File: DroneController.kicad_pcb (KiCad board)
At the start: 4 copper layers, 50.7 x 56.1 mm, 45 parts, among them J1 Connector, J2 Connector, J3 Connector, P1 USB_C_Plug, SW1 SW_SPDT, U2 W25Q16JVSS, U3 BMP280, U4 MPU-6500, U6 L86-M33, U7 915MHz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

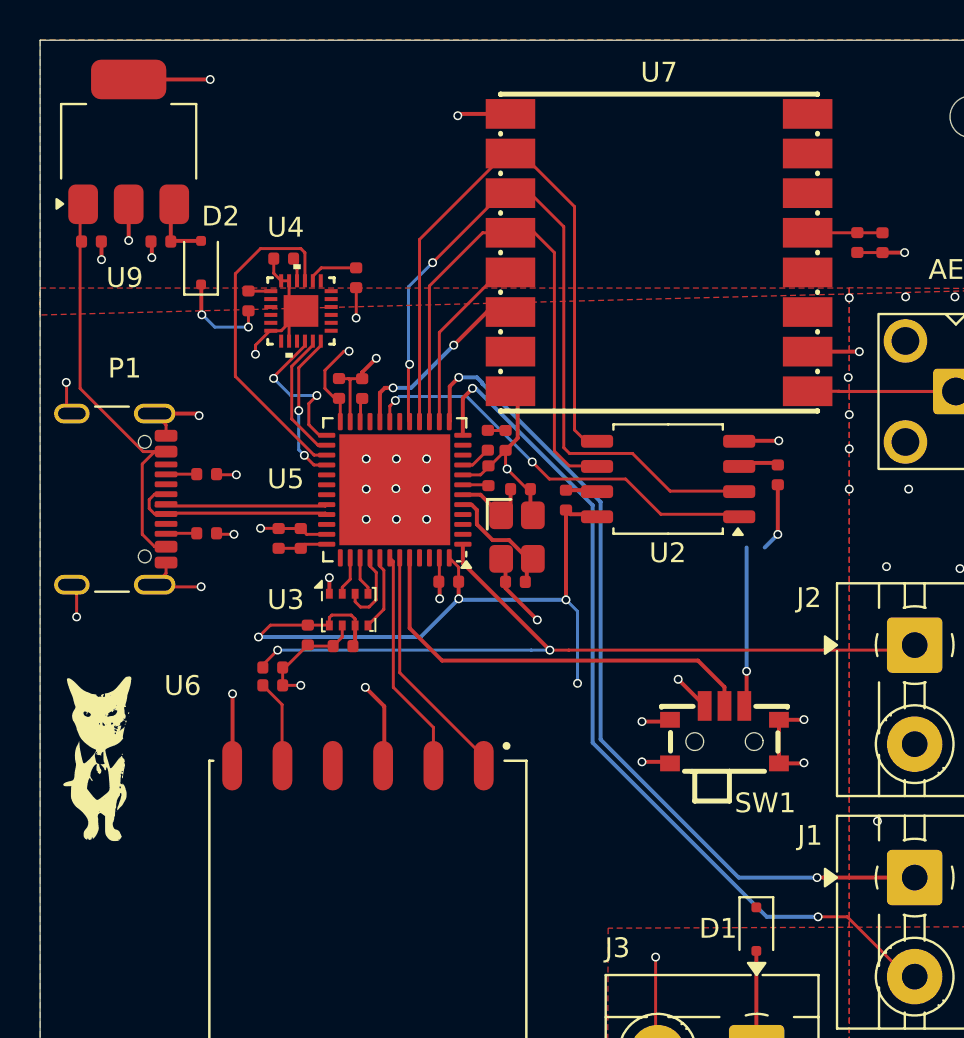
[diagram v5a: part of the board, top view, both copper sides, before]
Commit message: Updated DRC requirements, footprints, and board stackup for impedance management
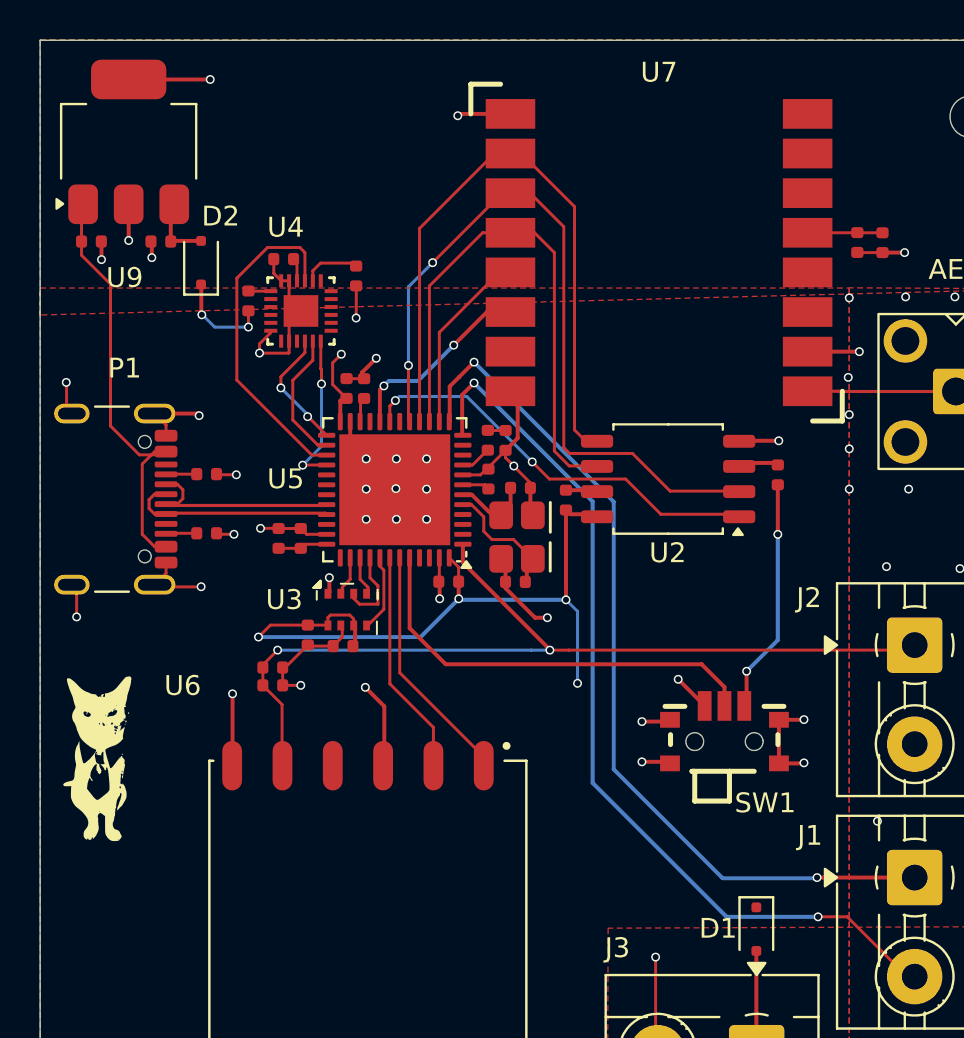
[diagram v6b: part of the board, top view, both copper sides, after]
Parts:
- moved C9 0.38 mm to (116.9, 122.4)
- moved C27 0.17 mm to (124.0, 127.0)
- moved C26 0.10 mm to (117.8, 122.4)
- moved C1 0.09 mm to (117.3, 116.8)
- moved U3 0.07 mm to (116.9, 133.6)
- moved C7 0.06 mm to (125.6, 127.5)
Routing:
- net GND: track 100.7 -> 103.3 mm
- net /USB_FS_DN: track 8.75 -> 10.6 mm
- net /USART2_TX: track 44.2 -> 45.9 mm
- net /SPI2_NSS: track 7.84 -> 6.22 mm
- net /USART2_RX: track 43.0 -> 44.5 mm
- net +BATT: track 45.2 -> 46.1 mm
- net /USB_FS_DP: track 11.2 -> 10.5 mm

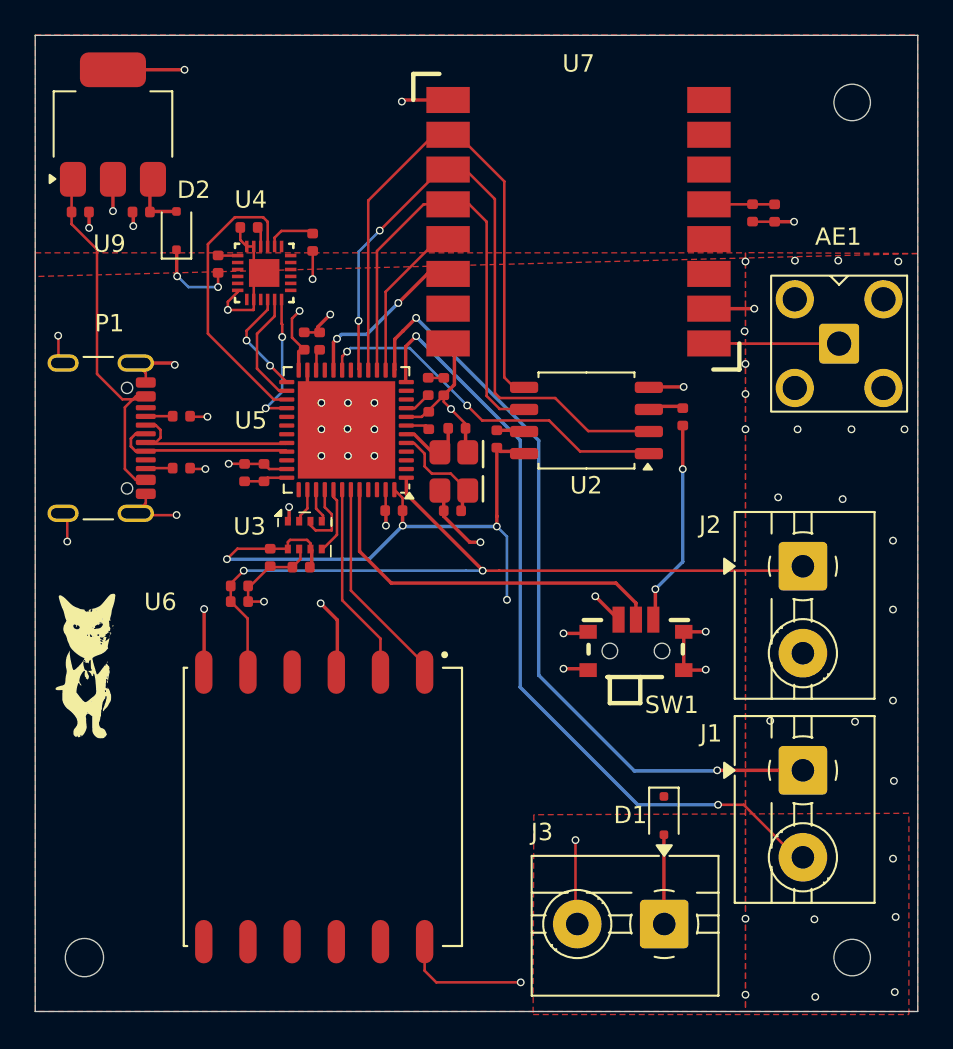
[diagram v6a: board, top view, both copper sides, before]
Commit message: added pull-up resistors, added keepout zones.
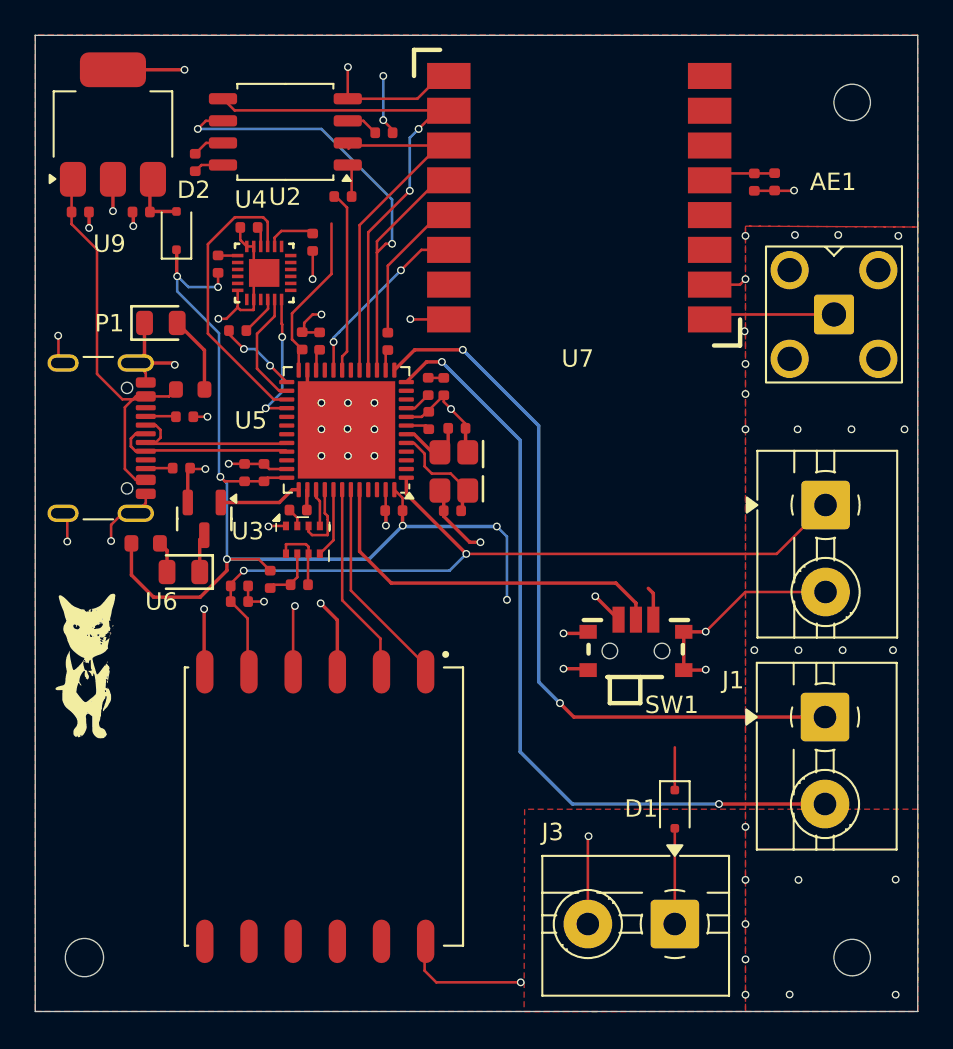
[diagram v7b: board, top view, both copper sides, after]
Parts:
- added D3: Green, PCM_JLCPCB:D_0805, F.Cu at (108.6, 121.4)
- added D5: Red, PCM_JLCPCB:D_0805, F.Cu at (109.9, 135.7)
- added Q2: AO3400A, PCM_JLCPCB:Q_SOT-23, F.Cu at (111.1, 132.7)
- added R10: 5.1kΩ, PCM_JLCPCB:R_0402, F.Cu at (121.7, 122.5)
- added R5: 75Ω, PCM_JLCPCB:R_0603, F.Cu at (107.7, 134.1)
- added R6: 75Ω, PCM_JLCPCB:R_0603, F.Cu at (110.3, 125.2)
- added R7: 5.1kΩ, PCM_JLCPCB:R_0402, F.Cu at (119.1, 114.1)
- added R8: 5.1kΩ, PCM_JLCPCB:R_0402, F.Cu at (116.5, 132.1)
- added R9: 5.1kΩ, PCM_JLCPCB:R_0402, F.Cu at (113.0, 121.8)
- moved U2 24.0 mm to (115.8, 110.4)
- moved R3 23.7 mm to (121.4, 110.5), turned to 0 degrees
- moved R4 23.5 mm to (110.6, 112.2)
- moved J2 3.75 mm to (146.8, 131.9)
- moved J1 3.32 mm to (146.8, 144.1)
- moved C28 1.79 mm to (143.9, 113.3)
- moved C5 1.77 mm to (142.7, 113.3)
- moved AE1 1.70 mm to (147.3, 120.9)
- moved U7 1.38 mm to (132.7, 114.2)
- moved C12 1.26 mm to (114.9, 136.1)
- moved C17 1.02 mm to (116.6, 136.4)
- moved D1 0.73 mm to (138.2, 149.4)
- moved J3 0.61 mm to (138.2, 156.0)
- moved U3 0.29 mm to (116.8, 133.9)
- moved R1 0.19 mm to (110.0, 126.8)
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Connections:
- U2 pad 1: /SPI5_NSS -> Net-(U2-~{CS})
- U3 pad 2: /SPI3_NSS -> Net-(U3-CSB)
- U4 pad 22: /SPI2_NSS -> Net-(U4-nCS)
- U5 pad 37: unconnected-(U5-PA14-Pad37) -> Net-(Q2-G)
- U7 pad 5: /SPI1_NSS -> Net-(U7-NSS)
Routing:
- net +3.3V: track 66.7 -> 91.6 mm
- net /SPI1_MOSI: track 37.7 -> 21.2 mm, vias 2 -> 0
- net GND: track 103.3 -> 118.3 mm, vias 67 -> 65
- net /SPI5_NSS: track 21.1 -> 10.5 mm, vias 2 -> 0
- net Net-(U7-NSS): track 0.00 -> 8.56 mm
- net /SPI1_NSS: track 9.35 -> 1.20 mm
- net Net-(Q2-G): track 0.00 -> 4.78 mm
- net /SPI1_SCK: track 26.6 -> 31.1 mm, vias 0 -> 2
- net Net-(D3-Pad2): track 0.00 -> 4.47 mm
- net 3.3V: track 0.00 -> 3.83 mm, vias 0 -> 1
- net Net-(U4-nCS): track 0.00 -> 2.44 mm
- net Net-(Q2-D): track 0.00 -> 2.23 mm
- net Net-(U2-~{CS}): track 0.00 -> 1.90 mm
- net +5V: track 21.8 -> 23.7 mm
- net /USART2_RX: track 44.5 -> 42.6 mm
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
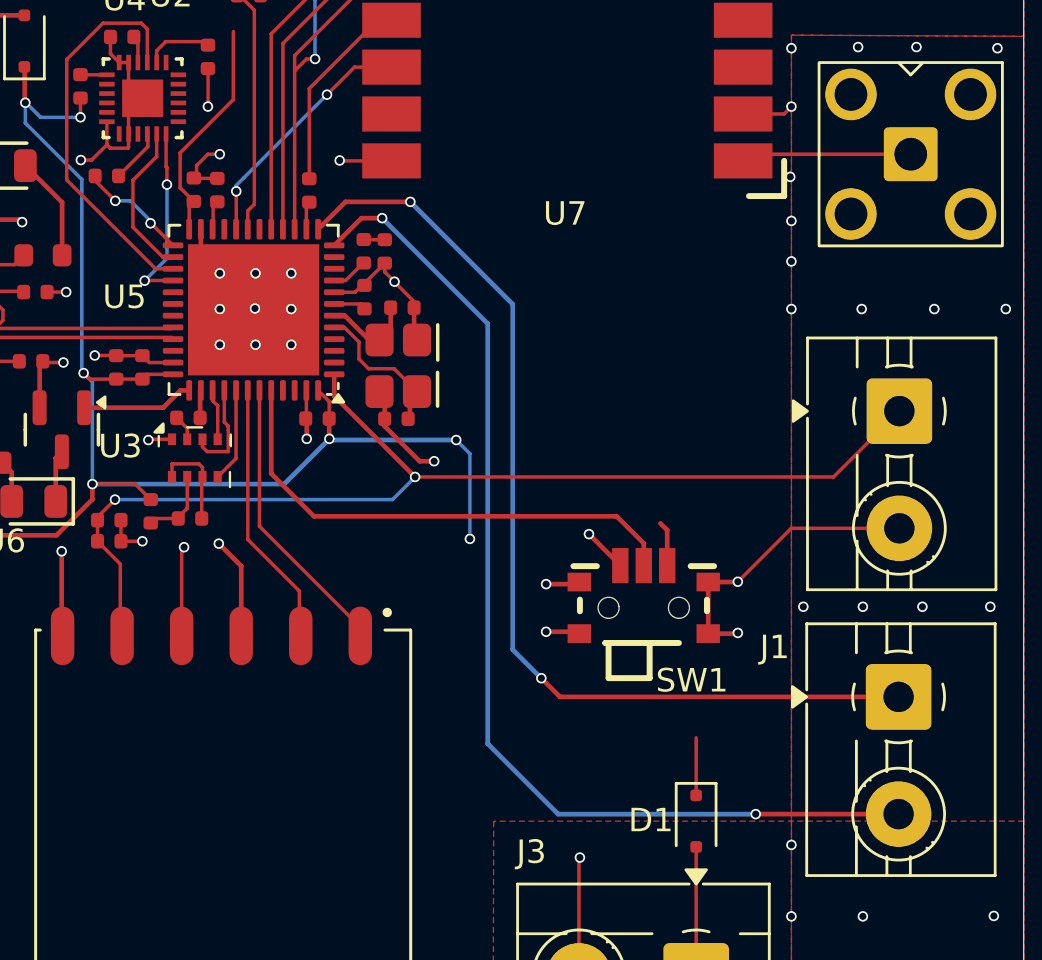
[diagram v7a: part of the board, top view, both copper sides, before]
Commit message: Fixed GPS wiring
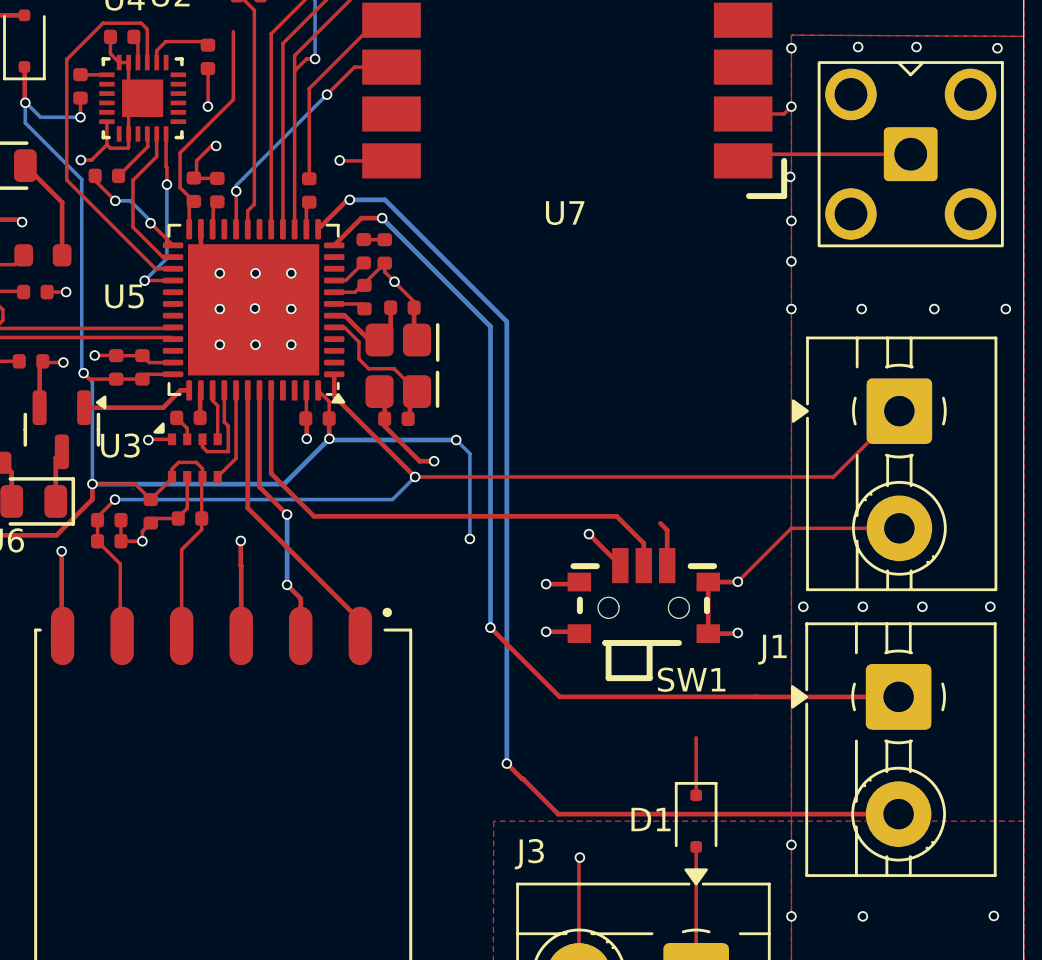
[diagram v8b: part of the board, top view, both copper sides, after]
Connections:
- J1 pad 1: /USART2_RX -> /MCU_TX2
- J1 pad 2: /USART2_TX -> /MCU_RX2
- U5 pad 12: /USART2_TX -> /MCU_TX2
- U5 pad 13: /USART2_RX -> /MCU_RX2
- U5 pad 42: /USART1_TX -> /MCU_TX1
- U5 pad 43: /USART1_RX -> /MCU_RX1
- U6 pad 1: /USART1_RX -> /MCU_TX1
- U6 pad 2: /USART1_TX -> /MCU_RX1
- U6 pad 4: 3.3V -> +3.3V
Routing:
- net /MCU_RX2: track 0.00 -> 47.2 mm, vias 0 -> 2
- net /USART2_TX: track 45.6 -> 0.00 mm, vias 2 -> 0
- net /USART2_RX: track 42.6 -> 0.00 mm, vias 2 -> 0
- net /MCU_TX2: track 0.00 -> 40.5 mm, vias 0 -> 2
- net /MCU_TX1: track 0.00 -> 12.5 mm
- net /USART1_RX: track 12.3 -> 0.00 mm
- net /USART1_TX: track 11.5 -> 0.00 mm
- net /MCU_RX1: track 0.00 -> 11.2 mm, vias 0 -> 2
- net +3.3V: track 91.6 -> 98.2 mm
- net 3.3V: track 3.83 -> 0.00 mm, vias 1 -> 0
- net GND: track 118.3 -> 119.1 mm
